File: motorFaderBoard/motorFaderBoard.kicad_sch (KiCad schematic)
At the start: 18 parts, among them J1 Conn_01x08_Pin, J2 Conn_01x08_Socket, U1 ADS1115IDGS, U2 PCF8574T, U3 L293DD

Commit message: pcb and stuff
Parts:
- removed C5: 100nF, Capacitor_SMD:C_0805_2012Metric_Pad1.18x1.45mm_HandSolder, symbol Device:C
- removed J1: Conn_01x08_Pin, symbol Connector:Conn_01x08_Pin
- removed J2: Conn_01x08_Socket, symbol Connector:Conn_01x08_Socket
- removed JP1, JP10, JP2, JP3, JP4, JP5, JP6, JP7, JP8, JP9: SolderJumper_2_Open, Jumper:SolderJumper-2_P1.3mm_Open_RoundedPad1.0x1.5mm, symbol Jumper:SolderJumper_2_Open
- removed U1: ADS1115IDGS, Package_SO:TSSOP-10_3x3mm_P0.5mm, symbol Analog_ADC:ADS1115IDGS
- removed U2: PCF8574T, Package_SO:SOIC-16W_7.5x10.3mm_P1.27mm, symbol Interface_Expansion:PCF8574T
- added A1: Arduino_Nano_v3.x, Module:Arduino_Nano, symbol MCU_Module:Arduino_Nano_v3.x
- added A2: Arduino_Leonardo, Module:Arduino_UNO_R3, symbol MCU_Module:Arduino_Leonardo
- added J1, J2: Conn_01x04_Pin, Connector_PinHeader_2.54mm:PinHeader_1x04_P2.54mm_Vertical, symbol Connector:Conn_01x04_Pin
- added J3, J4: Conn_01x04_Socket, Connector_PinSocket_2.54mm:PinSocket_1x04_P2.54mm_Vertical, symbol Connector:Conn_01x04_Socket
- added J5, J6: Conn_01x15_Socket, Connector_PinSocket_2.54mm:PinSocket_1x15_P2.54mm_Vertical_SMD_Pin1Right, symbol Connector:Conn_01x15_Socket
- added J7: Conn_01x06_Socket, Connector_PinSocket_2.54mm:PinSocket_1x05_P2.54mm_Vertical, symbol Connector:Conn_01x06_Socket
- added J8: Conn_01x03_Socket, Connector_PinSocket_2.54mm:PinSocket_1x03_P2.54mm_Vertical, symbol Connector:Conn_01x03_Socket
- added J9: Conn_01x03_Pin, Connector_PinHeader_2.54mm:PinHeader_1x03_P2.54mm_Vertical, symbol Connector:Conn_01x03_Pin
- added JP1, JP2, JP3, JP4: SolderJumper_3_Open, Jumper:SolderJumper-3_P2.0mm_Open_TrianglePad1.0x1.5mm, symbol Jumper:SolderJumper_3_Open
- added U1: ATmega328PB-A, Package_QFP:TQFP-32_7x7mm_P0.8mm, symbol MCU_Microchip_ATmega:ATmega328PB-A
- RV1, RV2: footprint (none) -> MotorFader:RES-TH_L146.5-W18.0_RSA0N11M9A07
- U3: footprint L293DD:SOIC127P1032X265-20N -> Package_SO:Infineon_SOIC-20W_7.6x12.8mm_P1.27mm
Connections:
- net +9V: now also J8.3 (Pin_3), J9.3 (Pin_3)
- net Fader1: now also RV1.2, A1.25 (A6), A2.11 (A2), J6.6 (Pin_6), U1.19 (PE2); no longer RV1. (1)
- net Fader2: now also RV2.2, A1.26 (A7), A2.12 (A3), J6.5 (Pin_5), U1.22 (PE3); no longer RV2. (1)
- net GND: now also RV1.1, RV2.1, A1.18 (AREF), A1.29 (GND), A1.4 (GND), A2.29 (GND), A2.30 (AREF), A2.6 (GND), A2.7 (GND), J1.1 (Pin_1), J2.1 (Pin_1), J3.1 (Pin_1), J4.1 (Pin_1), J5.4 (Pin_4), J6.13 (Pin_13), J6.2 (Pin_2), J7.1 (Pin_1), J8.1 (Pin_1), J9.1 (Pin_1), JP1.1 (A), JP2.1 (A), JP3.1 (A), JP4.1 (A), U1.20 (AREF), U1.21 (GND), U1.5 (GND); no longer RV1. (1), RV2. (1)
- net M1A: now also RV1.A; no longer RV1. (1), U3.13 (OUTPUT_3)
- net M1A_I: now also A1.10 (D7), A2.22 (D7), J5.10 (Pin_10), U1.11 (PD7); no longer U3.12 (INPUT_3)
- net M1B: now also RV1.B; no longer RV1. (1), U3.18 (OUTPUT_4)
- net M1B_I: now also A1.11 (D8), A2.23 (D8), J5.11 (Pin_11), U1.12 (PB0); no longer U3.19 (INPUT_4)
- net M2A: now also RV2.A, U3.13 (OUTPUT_3); no longer RV2. (1)
- net M2B: now also RV2.B, U3.18 (OUTPUT_4); no longer RV2. (1)
- net SCL: now also A1.24 (A5), A2.14 (A5), J1.4 (Pin_4), J2.4 (Pin_4), J3.4 (Pin_4), J4.4 (Pin_4), J6.7 (Pin_7), U1.28 (PC5)
- net SDA: now also A1.23 (A4), A2.13 (A4), J1.3 (Pin_3), J2.3 (Pin_3), J3.3 (Pin_3), J4.3 (Pin_3), J6.8 (Pin_8), U1.27 (PC4)
- net T1: now also RV1.T; no longer RV1. (1)
- net T2: now also RV2.T; no longer RV2. (1)
- net VCC: now also RV1.3, RV2.3, A1.27 (+5V), A2.5 (+5V), J1.2 (Pin_2), J2.2 (Pin_2), J3.2 (Pin_2), J4.2 (Pin_2), J6.4 (Pin_4), J7.3 (Pin_3), J8.2 (Pin_2), J9.2 (Pin_2), JP1.3 (B), JP2.3 (B), JP3.3 (B), JP4.3 (B), U1.18 (AVCC), U1.4 (VCC); no longer RV1. (1), RV2. (1), U3.1 (ENABLE_1), U3.11 (ENABLE_2)
- new net ADDR_1: A1.12 (D9), A2.24 (D9), J5.12 (Pin_12), JP1.2 (C), U1.13 (PB1)
- new net ADDR_2: A1.13 (D10), A2.25 (D10), J5.13 (Pin_13), JP2.2 (C), U1.14 (PB2)
- new net ADDR_4: A1.14 (D11), A2.26 (D11), J5.14 (Pin_14), JP3.2 (C), U1.15 (PB3)
- new net ADDR_8: A1.15 (D12), A2.27 (D12), J5.15 (Pin_15), JP4.2 (C), U1.16 (PB4)
- new net M1E: A1.9 (D6), A2.21 (D6), J5.9 (Pin_9), U1.10 (PD6), U3.1 (ENABLE_1)
- new net M2A_I: A1.7 (D4), A2.19 (D4), J5.7 (Pin_7), U1.2 (PD4), U3.12 (INPUT_3)
- new net M2B_I: A1.8 (D5), A2.20 (D5), J5.8 (Pin_8), U1.9 (PD5), U3.19 (INPUT_4)
- new net M2E: A1.6 (D3), A2.18 (D3/SCL), J5.6 (Pin_6), U1.1 (PD3), U3.11 (ENABLE_2)
- new net RX: A1.2 (D0/RX), J5.2 (Pin_2), J7.4 (Pin_4)
- new net TX: A1.1 (D1/TX), J5.1 (Pin_1), J7.5 (Pin_5)
- no-connect marks 4 -> 33
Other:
- note added: "I2C Addressing Solder Jumper"
- moved on the sheet: U3

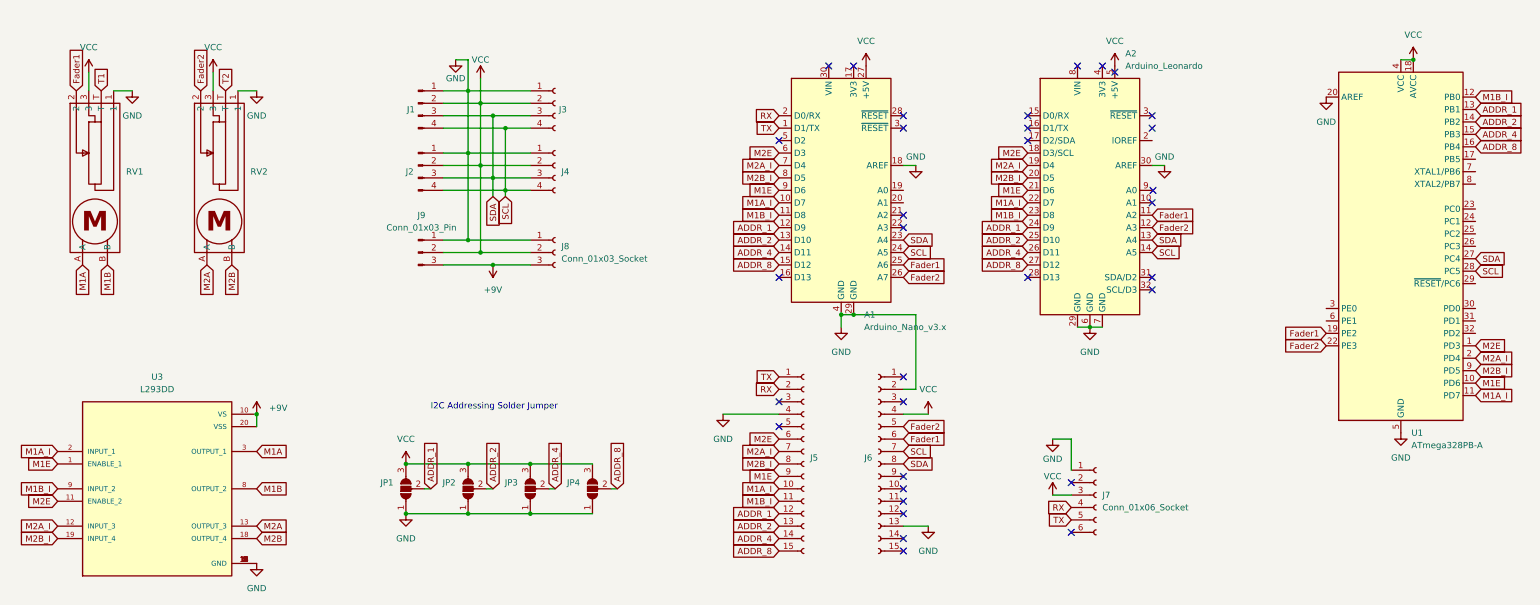
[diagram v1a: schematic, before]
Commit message: connectors, labels, vias
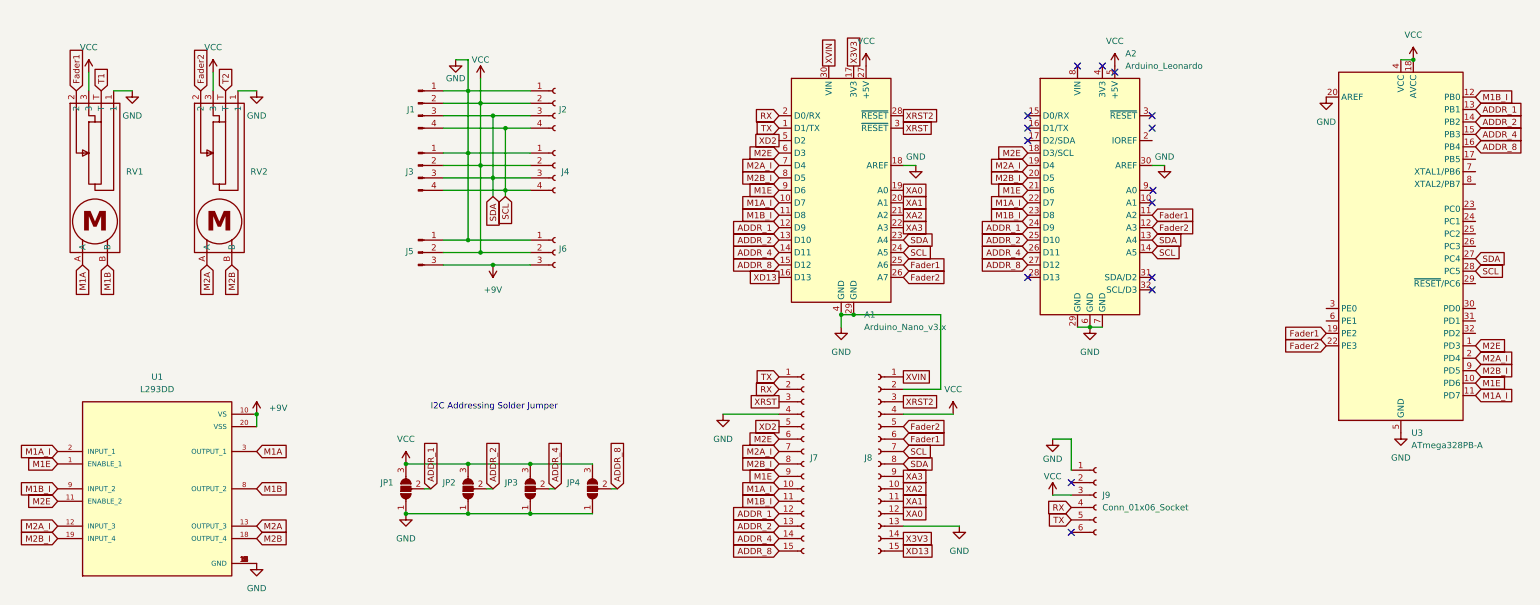
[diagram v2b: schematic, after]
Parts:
- A2: now left out of the parts list
- J9: renamed from J7; footprint Connector_PinSocket_2.54mm:PinSocket_1x05_P2.54mm_Vertical -> Connector_PinSocket_2.54mm:PinSocket_1x06_P2.54mm_Vertical
- U3: renamed from U1; now left out of the parts list
- renumbered J3 to J2, J2 to J3, J9 to J5, J8 to J6, J5 to J7, J6 to J8, U3 to U1
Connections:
- net XVIN: now reaches J8.1 (Pin_1)
- net XVIN: now also A1.30 (VIN)
- net XA2: now reaches J8.10 (Pin_10)
- net XA2: now also A1.21 (A2)
- net XA1: now reaches J8.11 (Pin_11)
- net XA1: now also A1.20 (A1)
- net XA0: now reaches J8.12 (Pin_12)
- net XA0: now also A1.19 (A0)
- net X3V3: now reaches J8.14 (Pin_14)
- net X3V3: now also A1.17 (3V3)
- net XD13: now reaches J8.15 (Pin_15)
- net XD13: now also A1.16 (D13)
- net XRST2: now reaches J8.3 (Pin_3)
- net XRST2: now also A1.28 (~{RESET})
- net XA3: now reaches J8.9 (Pin_9)
- net XA3: now also A1.22 (A3)
- net XRST: now reaches J7.3 (Pin_3)
- net XRST: now also A1.3 (~{RESET})
- net XD2: now reaches J7.5 (Pin_5)
- net XD2: now also A1.5 (D2)
- no-connect marks 33 -> 15
